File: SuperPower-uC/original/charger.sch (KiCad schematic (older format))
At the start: 30 parts, among them J4 DNP/JST_ZH_S2B_thru, J5 JST_XH_S2B_thru, Q12 DMP2035UVT, Q3 DMN3018SSD, Q4 2N7002A, U4 LTC4162EUFD-LAD

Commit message: Add JST ZH 3D Model
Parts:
- J4: footprint Connector_JST_user:JST_ZH_S2B-ZR_1x02_P1.50mm_Horizontal -> JST_ZH_S2B_THRU:JST_ZH_S2B-ZR_1x02_P1.50mm_Horizontal
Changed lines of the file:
@@
 F 0 "J4" H 8930 5942 50  0000 L CNN
 F 1 "DNP/JST_ZH_S2B_thru" H 8930 5851 50  0000 L CNN
-F 2 "Connector_JST_user:JST_ZH_S2B-ZR_1x02_P1.50mm_Horizontal" H 8850 5950 50  0001 C CNN
+F 2 "JST_ZH_S2B_THRU:JST_ZH_S2B-ZR_1x02_P1.50mm_Horizontal" H 8850 5950 50  0001 C CNN
 F 3 "http://www.jst-mfg.com/product/pdf/eng/eZH.pdf" H 8850 5950 50  0001 C CNN
 F 4 "JST" H 8850 5950 50  0001 C CNN "Mfr_name"

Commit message: Update DMN3018SSD SO-8 3D Package
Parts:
- Q3: footprint Package_SO:SO-8_3.9x4.9mm_P1.27mm -> DMN3018SSD:SO-8_3.9x4.9mm_P1.27mm
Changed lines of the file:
@@
 F 0 "Q3" V 4707 2925 50  0000 C CNN
 F 1 "DMN3018SSD" V 4616 2925 50  0000 C CNN
-F 2 "Package_SO:SO-8_3.9x4.9mm_P1.27mm" H 4350 2825 50  0001 L CNN
+F 2 "DMN3018SSD:SO-8_3.9x4.9mm_P1.27mm" H 4350 2825 50  0001 L CNN
 F 3 "https://www.diodes.com/assets/Datasheets/DMN3018SSD.pdf" H 4150 2900 50  0001 C CNN
 F 4 "Diodes Incorporated" H 4150 2900 50  0001 C CNN "Mfr_name"
@@
 F 0 "Q3" H 7588 3512 50  0000 L CNN
 F 1 "DMN3018SSD" H 7588 3421 50  0000 L CNN
-F 2 "Package_SO:SO-8_3.9x4.9mm_P1.27mm" H 7550 3275 50  0001 L CNN
+F 2 "DMN3018SSD:SO-8_3.9x4.9mm_P1.27mm" H 7550 3275 50  0001 L CNN
 F 3 "https://www.diodes.com/assets/Datasheets/DMN3018SSD.pdf" H 7350 3350 50  0001 C CNN
 F 4 "Diodes Incorporated" H 7350 3350 50  0001 C CNN "Mfr_name"

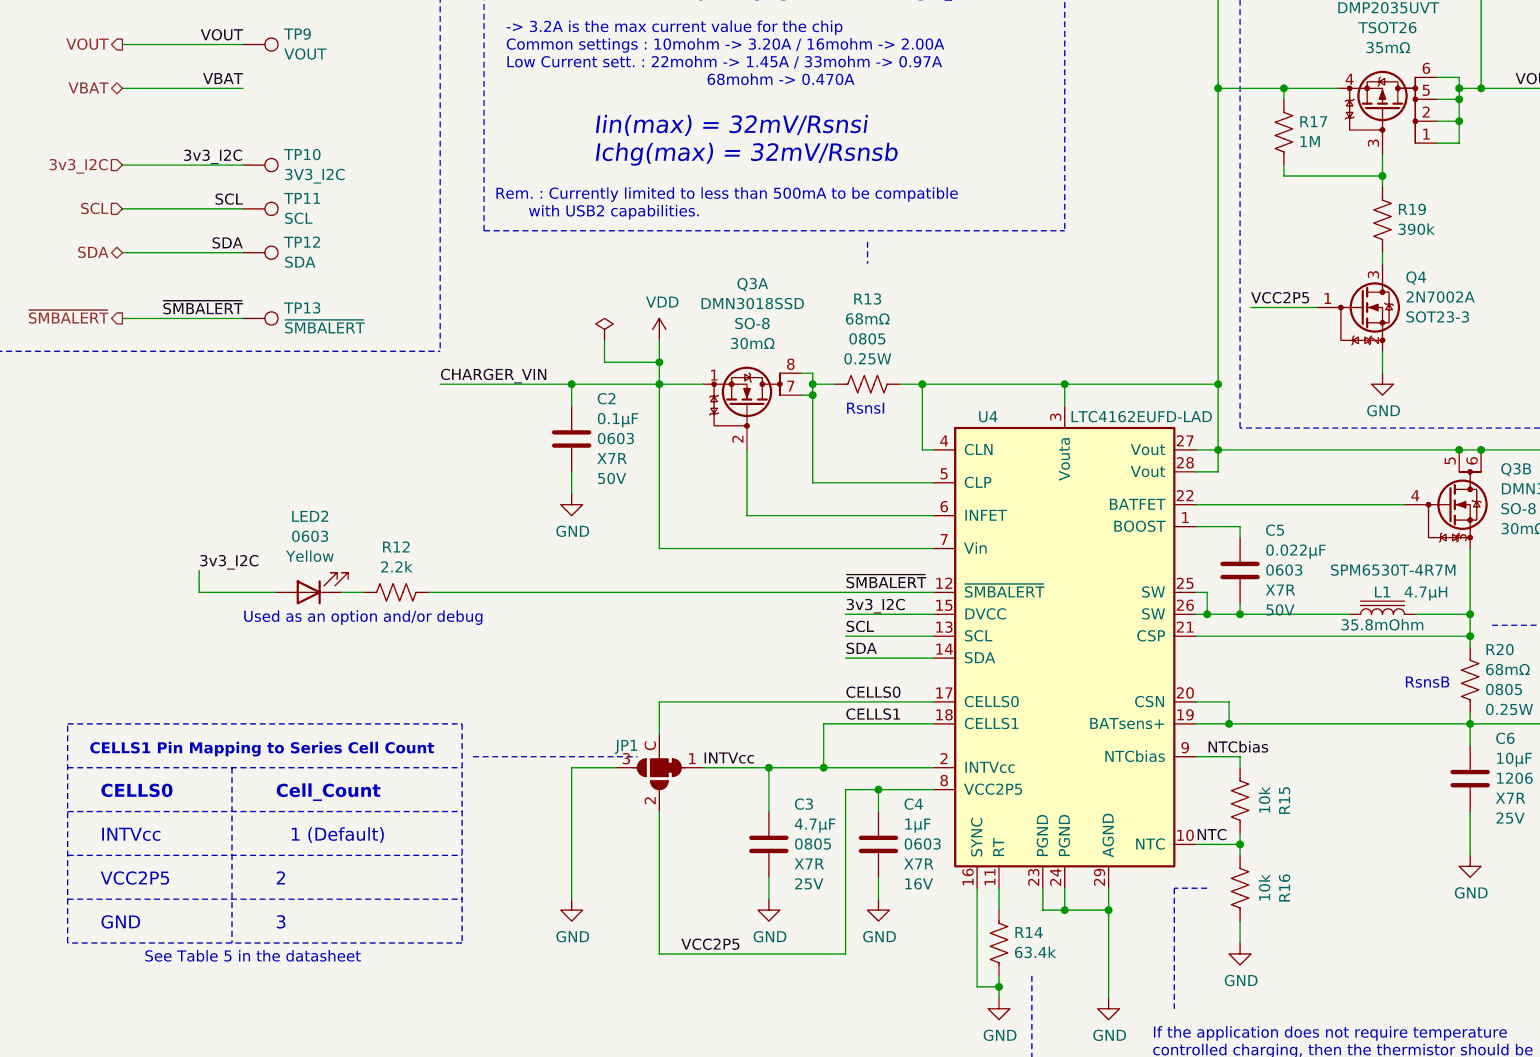
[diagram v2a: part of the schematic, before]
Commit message: Update LTC4162-L components placement
+ Misc.
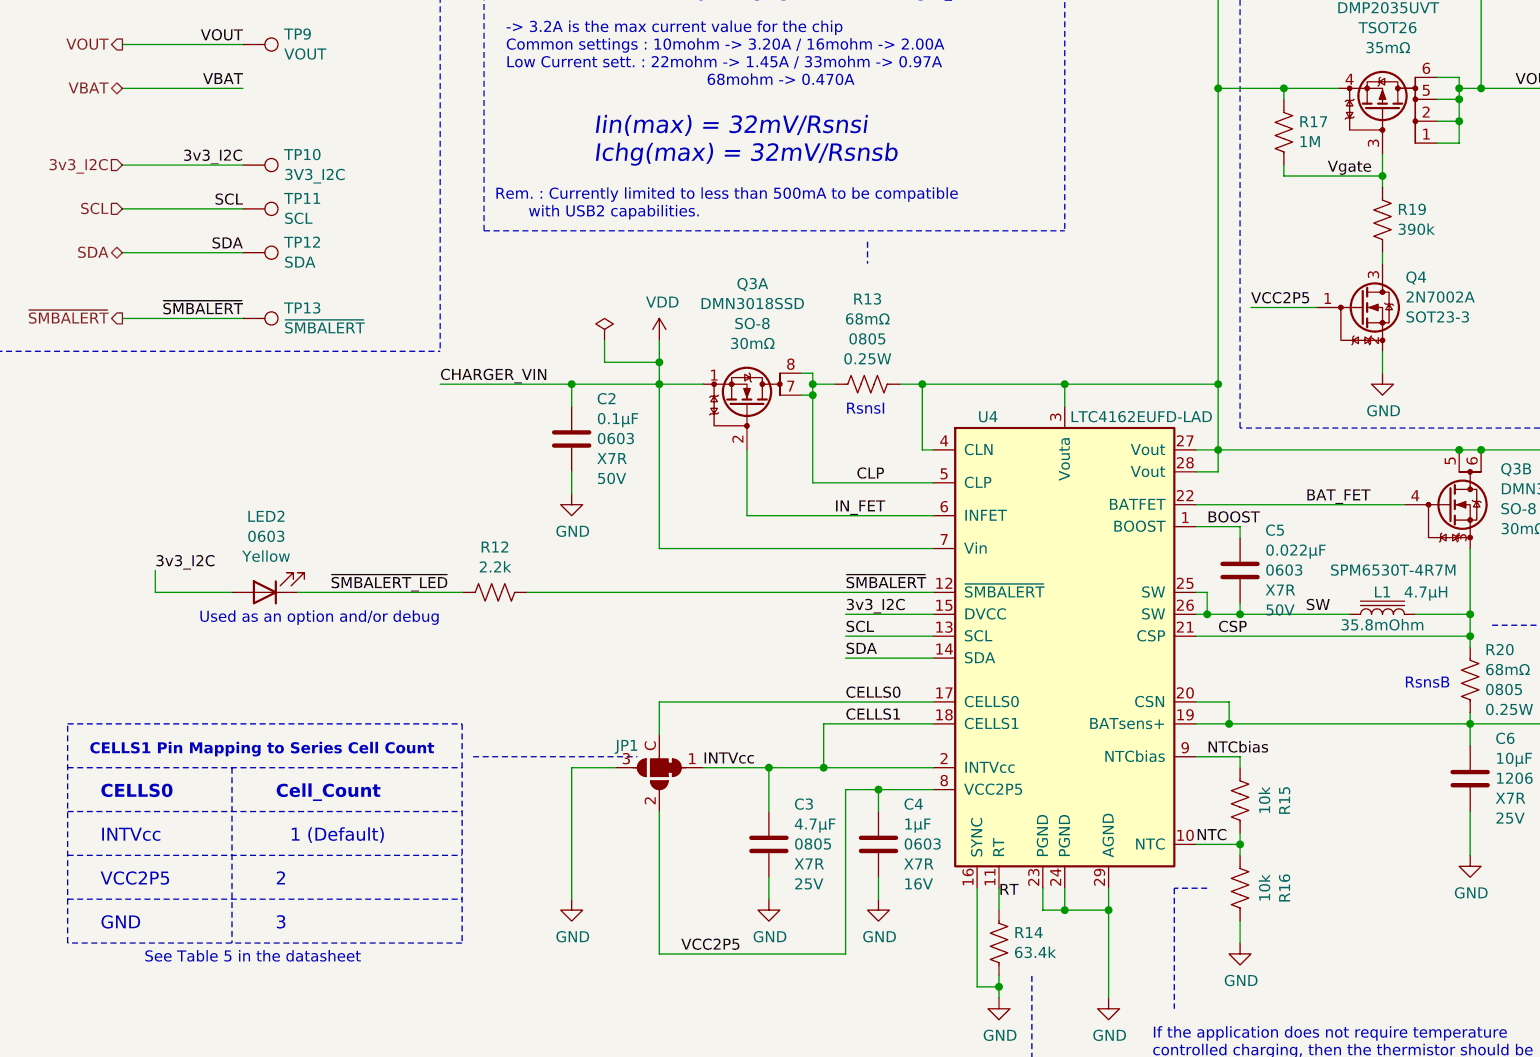
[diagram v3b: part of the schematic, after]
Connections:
- net RT: now reaches R14.2, U4.11 (RT)
- net ~SMBALERT_LED: now reaches LED2.1 (K), R12.2
- net Vgate: now reaches Q12.3 (G), R17.2, R19.1
- net BOOST: now reaches C5.1, U4.1 (BOOST)
- net CSP: now reaches L1.2, Q3.3 (S), R20.2, U4.21 (CSP)
- net BAT_FET: now reaches Q3.4 (G), U4.22 (BATFET)
- net SW: now reaches C5.2, L1.1, U4.25 (SW), U4.26 (SW)
- net CLP: now reaches Q3.7 (D), Q3.8 (D), R13.2, U4.5 (CLP)
- net IN_FET: now reaches Q3.2 (G), U4.6 (INFET)
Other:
- moved on the sheet: LED2, R12
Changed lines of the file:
@@
 L Device:R_US R12
 U 1 1 5F84595F
-P 2550 3750
-F 0 "R12" V 2345 3750 50  0000 C CNN
-F 1 "2.2k" V 2436 3750 50  0000 C CNN
-F 2 "Resistor_SMD:R_0603_1608Metric" V 2590 3740 50  0001 C CNN
-F 3 "~" H 2550 3750 50  0001 C CNN
-	1    2550 3750
+P 3000 3750
+F 0 "R12" V 2795 3750 50  0000 C CNN
+F 1 "2.2k" V 2886 3750 50  0000 C CNN
+F 2 "Resistor_SMD:R_0603_1608Metric" V 3040 3740 50  0001 C CNN
+F 3 "~" H 3000 3750 50  0001 C CNN
+	1    3000 3750
 	0    1    1    0
 $EndComp
 Wire Wire Line
-	5000 3750 2700 3750
-Wire Wire Line
-	2300 3750 2400 3750
-Wire Wire Line
-	2000 3750 1650 3750
-Wire Wire Line
-	1650 3750 1650 3650
-Text Notes 1850 3900 0    50   ~ 0
+	5000 3750 3150 3750
+Wire Wire Line
+	2100 3750 2850 3750
+Wire Wire Line
+	1800 3750 1450 3750
+Wire Wire Line
+	1450 3750 1450 3650
+Text Notes 1650 3900 0    50   ~ 0
 Used as an option and/or debug
 Wire Wire Line
@@
 	7400 1500 7400 1450
 Connection ~ 7400 1450
-Text Label 1650 3650 0    50   ~ 0
+Text Label 1450 3650 0    50   ~ 0
 3v3_I2C
 Text Notes 3450 1800 0    79   Italic 0
@@
 L 150060ys75000:150060YS75000_0603 LED2
 U 1 1 5FCED4FE
-P 2150 3750
-F 0 "LED2" H 2143 3405 50  0000 C CNN
-F 1 "150060YS75000_0603" H 2150 3650 50  0001 C CNN
-F 2 "LED_SMD:LED_0603_1608Metric" H 2150 3750 50  0001 C CNN
-F 3 "https://www.we-online.com/catalog/datasheet/150060YS75000.pdf" H 2150 3750 50  0001 C CNN
-F 4 "Wurth Elektronik " H 2150 3750 50  0001 C CNN "Mfr_name"
-F 5 "150060YS75000" H 2150 3750 50  0001 C CNN "Mfr_no"
-F 6 "0603" H 2143 3496 50  0000 C CNN "Package"
-F 7 "Yellow" H 2143 3587 50  0000 C CNN "Color"
-F 8 "https://octopart.com/search?autosugg_idx=0&currency=USD&oq=150060YS75000&q=150060YS75000&specs=1" H 2150 3750 50  0001 C CNN "Octopart_link"
-F 9 "https://fr.farnell.com/wurth-elektronik/150060ys75000/led-0603-jaune-120mcd-590nm/dp/2322074?st=150060ys75000" H 2150 3750 50  0001 C CNN "Farnell_link"
-F 10 "2322074" H 2150 3750 50  0001 C CNN "Farnell_ref"
-F 11 "2020-12-07" H 2150 3750 50  0001 C CNN "Farnell_check_date"
-F 12 "-" H 2150 3750 50  0001 C CNN "Farnell_price_qt=1"
-F 13 "0.139€" H 2150 3750 50  0001 C CNN "Farnell_price_qt=10"
-F 14 "0.115€" H 2150 3750 50  0001 C CNN "Farnell_price_qt=100"
-F 15 "0.0979€" H 2150 3750 50  0001 C CNN "Farnell_price_qt=1000"
-F 16 "15,254" H 2150 3750 50  0001 C CNN "Farnell_stock"
-F 17 "-" H 2150 3750 50  0001 C CNN "LCSC_link"
-F 18 "-" H 2150 3750 50  0001 C CNN "LCSC_ref"
-F 19 "2020-12-07" H 2150 3750 50  0001 C CNN "LCSC_check_date"
-F 20 "-" H 2150 3750 50  0001 C CNN "LCSC_price_qt=1"
-F 21 "-" H 2150 3750 50  0001 C CNN "LCSC_price_qt=10"
-F 22 "-" H 2150 3750 50  0001 C CNN "LCSC_price_qt=100"
-F 23 "-" H 2150 3750 50  0001 C CNN "LCSC_price_qt=1000"
-F 24 "-" H 2150 3750 50  0001 C CNN "LCSC_stock"
-F 25 "https://eu.mouser.com/ProductDetail/Wurth-Elektronik/150060YS75000?qs=LlUlMxKIyB0nKmwefHgtZw%3D%3D" H 2150 3750 50  0001 C CNN "Mouser_link"
-F 26 "710-150060YS75000 " H 2150 3750 50  0001 C CNN "Mouser_ref"
-F 27 "2020-12-07" H 2150 3750 50  0001 C CNN "Mouser_check_date"
-F 28 "$0.151" H 2300 3550 50  0001 C CNN "Mouser_price_qt=1"
-F 29 "$0.151" H 2300 3550 50  0001 C CNN "Mouser_price_qt=10"
-F 30 "$0.115" H 2300 3550 50  0001 C CNN "Mouser_price_qt=100"
-F 31 "$0.107" H 2300 3550 50  0001 C CNN "Mouser_price_qt=1000"
-F 32 "44,294" H 2150 3750 50  0001 C CNN "Mouser_stock"
-F 33 "https://fr.rs-online.com/web/p/led/8154219/" H 2150 3750 50  0001 C CNN "RS_link"
-F 34 "815-4219" H 2150 3750 50  0001 C CNN "RS_ref"
-F 35 "2020-12-07" H 2150 3750 50  0001 C CNN "RS_check_date"
-F 36 "-" H 2150 3750 50  0001 C CNN "RS_price_qt=1"
-F 37 "-" H 2150 3750 50  0001 C CNN "RS_price_qt=10"
-F 38 "0.101€" H 2150 3750 50  0001 C CNN "RS_price_qt=100"
-F 39 "0.074€" H 2150 3750 50  0001 C CNN "RS_price_qt=1000"
-F 40 "400" H 2150 3750 50  0001 C CNN "RS_stock"
-F 41 "TO_CHECK" H 2150 3750 50  0001 C CNN "Status"
-F 42 "1.00" H 2150 3750 50  0001 C CNN "Release_version"
-F 43 "2020-11-23" H 2150 3750 50  0001 C CNN "Release_date"
-F 44 "ManWithNoName" H 2150 3750 50  0001 C CNN "Designer"
-	1    2150 3750
+P 1950 3750
+F 0 "LED2" H 1943 3405 50  0000 C CNN
+F 1 "150060YS75000_0603" H 1950 3650 50  0001 C CNN
+F 2 "LED_SMD:LED_0603_1608Metric" H 1950 3750 50  0001 C CNN
+F 3 "https://www.we-online.com/catalog/datasheet/150060YS75000.pdf" H 1950 3750 50  0001 C CNN
+F 4 "Wurth Elektronik " H 1950 3750 50  0001 C CNN "Mfr_name"
+F 5 "150060YS75000" H 1950 3750 50  0001 C CNN "Mfr_no"
+F 6 "0603" H 1943 3496 50  0000 C CNN "Package"
+F 7 "Yellow" H 1943 3587 50  0000 C CNN "Color"
+F 8 "https://octopart.com/search?autosugg_idx=0&currency=USD&oq=150060YS75000&q=150060YS75000&specs=1" H 1950 3750 50  0001 C CNN "Octopart_link"
+F 9 "https://fr.farnell.com/wurth-elektronik/150060ys75000/led-0603-jaune-120mcd-590nm/dp/2322074?st=150060ys75000" H 1950 3750 50  0001 C CNN "Farnell_link"
+F 10 "2322074" H 1950 3750 50  0001 C CNN "Farnell_ref"
+F 11 "2020-12-07" H 1950 3750 50  0001 C CNN "Farnell_check_date"
+F 12 "-" H 1950 3750 50  0001 C CNN "Farnell_price_qt=1"
+F 13 "0.139€" H 1950 3750 50  0001 C CNN "Farnell_price_qt=10"
+F 14 "0.115€" H 1950 3750 50  0001 C CNN "Farnell_price_qt=100"
+F 15 "0.0979€" H 1950 3750 50  0001 C CNN "Farnell_price_qt=1000"
+F 16 "15,254" H 1950 3750 50  0001 C CNN "Farnell_stock"
+F 17 "-" H 1950 3750 50  0001 C CNN "LCSC_link"
+F 18 "-" H 1950 3750 50  0001 C CNN "LCSC_ref"
+F 19 "2020-12-07" H 1950 3750 50  0001 C CNN "LCSC_check_date"
+F 20 "-" H 1950 3750 50  0001 C CNN "LCSC_price_qt=1"
+F 21 "-" H 1950 3750 50  0001 C CNN "LCSC_price_qt=10"
+F 22 "-" H 1950 3750 50  0001 C CNN "LCSC_price_qt=100"
+F 23 "-" H 1950 3750 50  0001 C CNN "LCSC_price_qt=1000"
+F 24 "-" H 1950 3750 50  0001 C CNN "LCSC_stock"
+F 25 "https://eu.mouser.com/ProductDetail/Wurth-Elektronik/150060YS75000?qs=LlUlMxKIyB0nKmwefHgtZw%3D%3D" H 1950 3750 50  0001 C CNN "Mouser_link"
+F 26 "710-150060YS75000 " H 1950 3750 50  0001 C CNN "Mouser_ref"
+F 27 "2020-12-07" H 1950 3750 50  0001 C CNN "Mouser_check_date"
+F 28 "$0.151" H 2100 3550 50  0001 C CNN "Mouser_price_qt=1"
+F 29 "$0.151" H 2100 3550 50  0001 C CNN "Mouser_price_qt=10"
+F 30 "$0.115" H 2100 3550 50  0001 C CNN "Mouser_price_qt=100"
+F 31 "$0.107" H 2100 3550 50  0001 C CNN "Mouser_price_qt=1000"
+F 32 "44,294" H 1950 3750 50  0001 C CNN "Mouser_stock"
+F 33 "https://fr.rs-online.com/web/p/led/8154219/" H 1950 3750 50  0001 C CNN "RS_link"
+F 34 "815-4219" H 1950 3750 50  0001 C CNN "RS_ref"
+F 35 "2020-12-07" H 1950 3750 50  0001 C CNN "RS_check_date"
+F 36 "-" H 1950 3750 50  0001 C CNN "RS_price_qt=1"
+F 37 "-" H 1950 3750 50  0001 C CNN "RS_price_qt=10"
+F 38 "0.101€" H 1950 3750 50  0001 C CNN "RS_price_qt=100"
+F 39 "0.074€" H 1950 3750 50  0001 C CNN "RS_price_qt=1000"
+F 40 "400" H 1950 3750 50  0001 C CNN "RS_stock"
+F 41 "TO_CHECK" H 1950 3750 50  0001 C CNN "Status"
+F 42 "1.00" H 1950 3750 50  0001 C CNN "Release_version"
+F 43 "2020-11-23" H 1950 3750 50  0001 C CNN "Release_date"
+F 44 "ManWithNoName" H 1950 3750 50  0001 C CNN "Designer"
+	1    1950 3750
 	-1   0    0    1
 $EndComp
@@
 Connection ~ 7400 3100
 Connection ~ 7500 3100
+Text Label 4650 3250 0    50   ~ 0
+CLP
+Text Label 4550 3400 0    50   ~ 0
+IN_FET
+Text Label 5300 5150 0    50   ~ 0
+RT
+Text Label 6300 3950 0    50   ~ 0
+CSP
+Text Label 6700 3850 0    50   ~ 0
+SW
+Text Label 6250 3450 0    50   ~ 0
+BOOST
+Text Label 6700 3350 0    50   ~ 0
+BAT_FET
+Text Label 2250 3750 0    50   ~ 0
+~SMBALERT_LED
+Text Label 6800 1850 0    50   ~ 0
+Vgate
 $EndSCHEMATC

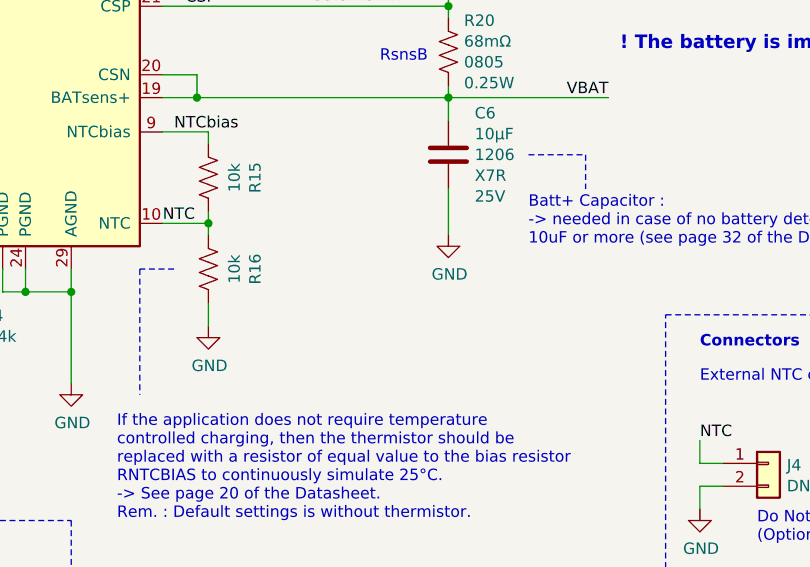
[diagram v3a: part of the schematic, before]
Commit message: Add some DIP switch 1 way (x3)
+ add optionnal on board 0603 NTC + misc.
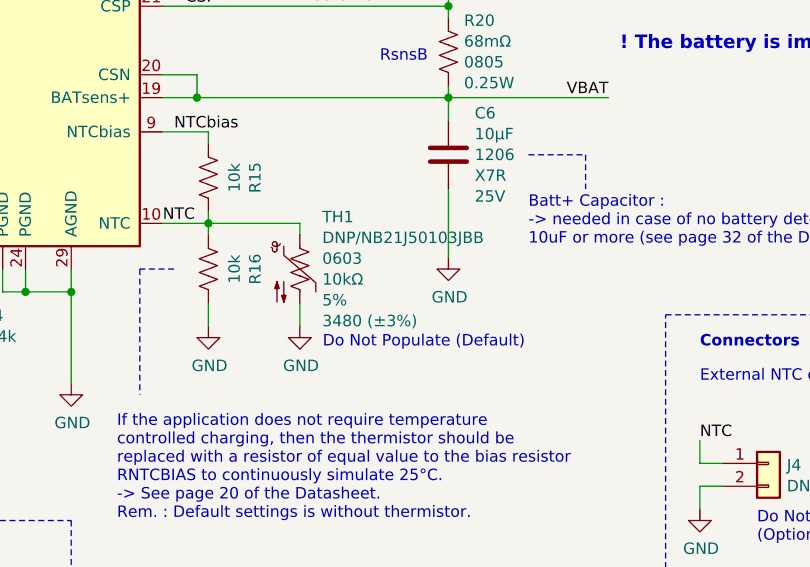
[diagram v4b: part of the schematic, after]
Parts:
- added TH1: DNP/NB21J50103JBB, Resistor_SMD:R_0603_1608Metric, symbol nb21j50103jbb:NB21J50103JBB
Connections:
- net GND: now also TH1.2
- net NTC: now also TH1.1
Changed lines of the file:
@@
 L power:GND #PWR033
 U 1 1 5F75816F
-P 7450 4950
-F 0 "#PWR033" H 7450 4700 50  0001 C CNN
-F 1 "GND" H 7455 4777 50  0000 C CNN
-F 2 "" H 7450 4950 50  0001 C CNN
-F 3 "" H 7450 4950 50  0001 C CNN
-	1    7450 4950
+P 7450 5050
+F 0 "#PWR033" H 7450 4800 50  0001 C CNN
+F 1 "GND" H 7455 4877 50  0000 C CNN
+F 2 "" H 7450 5050 50  0001 C CNN
+F 3 "" H 7450 5050 50  0001 C CNN
+	1    7450 5050
 	1    0    0    -1
 $EndComp
@@
 	7450 4350 8150 4350
 Wire Wire Line
-	7450 4750 7450 4950
+	7450 4750 7450 5050
 Text Notes 8550 5450 0    50   ~ 10
 Connectors
@@
 Text Label 6800 1850 0    50   ~ 0
 Vgate
+$Comp
+L nb21j50103jbb:NB21J50103JBB TH1
+U 1 1 60203657
+P 6800 5100
+F 0 "TH1" H 6898 5328 50  0000 L CNN
+F 1 "DNP/NB21J50103JBB" H 6898 5237 50  0000 L CNN
+F 2 "Resistor_SMD:R_0603_1608Metric" H 6800 5150 50  0001 C CNN
+F 3 "http://datasheets.avx.com/nb21-nb12-nb20.pdf" H 6800 5150 50  0001 C CNN
+F 4 "AVX" H 6800 5100 50  0001 C CNN "Mfr_name"
+F 5 "NB21J50103JBB" H 6800 5100 50  0001 C CNN "Mfr_no"
+F 6 "0603" H 6898 5146 50  0000 L CNN "Package"
+F 7 "CTN" H 6800 5100 50  0001 C CNN "thms_Type"
+F 8 "10kΩ" H 6898 5055 50  0000 L CNN "thms_Value"
+F 9 "5%" H 6898 4964 50  0000 L CNN "thms_Tolerance"
+F 10 "-55°C_to_+150°C" H 6800 5100 50  0001 C CNN "thms_Temp_Range"
+F 11 "4s" H 6800 5100 50  0001 C CNN "thms_Thermal_Time_Constant"
+F 12 "3480 (±3%)" H 6898 4873 50  0000 L CNN "thms_Beta_Constant"
+F 13 "https://octopart.com/nb21j50103jbb-avx-8449209?r=sp" H 6800 5100 50  0001 C CNN "Octopart_link"
+F 14 "https://fr.farnell.com/avx/nb21j50103jbb/thermistance-ctn-10k-0603/dp/1672340?st=NB21J50103JBB" H 6800 5100 50  0001 C CNN "Farnell_link"
+F 15 "1672340" H 6800 5100 50  0001 C CNN "Farnell_ref"
+F 16 "2020-12-21" H 6800 5100 50  0001 C CNN "Farnell_check_date"
+F 17 "-" H 6800 5100 50  0001 C CNN "Farnell_price_qt=1"
+F 18 "0,345 €" H 6800 5100 50  0001 C CNN "Farnell_price_qt=10"
+F 19 "0,273 €" H 6800 5100 50  0001 C CNN "Farnell_price_qt=100"
+F 20 "0,221 €" H 6800 5100 50  0001 C CNN "Farnell_price_qt=1000"
+F 21 "7,076" H 6800 5100 50  0001 C CNN "Farnell_stock"
+F 22 "-" H 6800 5100 50  0001 C CNN "LCSC_link"
+F 23 "-" H 6800 5100 50  0001 C CNN "LCSC_ref"
+F 24 "2020-12-21" H 6800 5100 50  0001 C CNN "LCSC_check_date"
+F 25 "-" H 6800 5100 50  0001 C CNN "LCSC_price_qt=1"
+F 26 "-" H 6800 5100 50  0001 C CNN "LCSC_price_qt=10"
+F 27 "-" H 6800 5100 50  0001 C CNN "LCSC_price_qt=100"
+F 28 "-" H 6800 5100 50  0001 C CNN "LCSC_price_qt=1000"
+F 29 "-" H 6800 5100 50  0001 C CNN "LCSC_stock"
+F 30 "https://eu.mouser.com/ProductDetail/AVX/NB21J50103JBB/?qs=%2Fha2pyFaduhUy%2FEg1uqHXntEXn44Wy%252BSIKjk0tx541cgq2JndSnUMg%3D%3D" H 6800 5100 50  0001 C CNN "Mouser_link"
+F 31 "Not Assigned" H 6800 5100 50  0001 C CNN "Mouser_ref"
+F 32 "2020-12-21" H 6800 5100 50  0001 C CNN "Mouser_check_date"
+F 33 "-" H 6800 5100 50  0001 C CNN "Mouser_price_qt=1"
+F 34 "-" H 6800 5100 50  0001 C CNN "Mouser_price_qt=10"
+F 35 "-" H 6800 5100 50  0001 C CNN "Mouser_price_qt=100"
+F 36 "-" H 6800 5100 50  0001 C CNN "Mouser_price_qt=1000"
+F 37 "-" H 6800 5100 50  0001 C CNN "Mouser_stock"
+F 38 "https://fr.rs-online.com/web/p/thermistances/6976758/" H 6800 5100 50  0001 C CNN "RS_link"
+F 39 "697-6758" H 6800 5100 50  0001 C CNN "RS_ref"
+F 40 "2020-12-21" H 6800 5100 50  0001 C CNN "RS_check_date"
+F 41 "-" H 6800 5100 50  0001 C CNN "RS_price_qt=1"
+F 42 "0,382 €" H 6800 5100 50  0001 C CNN "RS_price_qt=10"
+F 43 "0,288 €" H 6800 5100 50  0001 C CNN "RS_price_qt=100"
+F 44 "0,226 €" H 6800 5100 50  0001 C CNN "RS_price_qt=1000"
+F 45 "6,335" H 6800 5100 50  0001 C CNN "RS_stock"
+F 46 "TO_CHECK" H 6800 5100 50  0001 C CNN "Status"
+F 47 "1.00" H 6800 5100 50  0001 C CNN "Release_version"
+F 48 "2020-12-21" H 6800 5100 50  0001 C CNN "Release_date"
+F 49 "ManWithNoName" H 6800 5100 50  0001 C CNN "Designer"
+	1    6800 5100
+	1    0    0    -1
+$EndComp
+$Comp
+L power:GND #PWR057
+U 1 1 60205C13
+P 6800 5350
+F 0 "#PWR057" H 6800 5100 50  0001 C CNN
+F 1 "GND" H 6805 5177 50  0000 C CNN
+F 2 "" H 6800 5350 50  0001 C CNN
+F 3 "" H 6800 5350 50  0001 C CNN
+	1    6800 5350
+	1    0    0    -1
+$EndComp
+Wire Wire Line
+	6800 5250 6800 5350
+Wire Wire Line
+	6800 4950 6800 4900
+Wire Wire Line
+	6800 4900 6400 4900
+Text Notes 6900 5450 0    50   ~ 0
+Do Not Populate (Default)
 $EndSCHEMATC
